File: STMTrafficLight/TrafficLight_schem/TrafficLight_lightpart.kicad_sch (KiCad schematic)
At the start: 66 parts, among them U1 74HC595D, U2 74HC595D, U3 74HC595D

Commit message: Marked connectors and added power LEDs, fixed resistors
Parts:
- removed LED?: Red, LED_SMD:LED_0805_2012Metric, symbol Device:LED
- removed R?: 2k, Resistor_SMD:R_0603_1608Metric, symbol Device:R
- added LED?: Green, LED_SMD:LED_0805_2012Metric, symbol Device:LED
- added R?: 1k, Resistor_SMD:R_0805_2012Metric, symbol Device:R
- R?: value 2k -> 1k; footprint Resistor_SMD:R_0603_1608Metric -> Resistor_SMD:R_0805_2012Metric; Distributor link 1 https://www.mouser.se/ProductDetail/Royalohm/0603WAF2001T5E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 -> https://jlcpcb.com/partdetail/18201-0805W8F1001T5E/C17513; Distributor link 2 (none) -> https://www.mouser.se/ProductDetail/Royalohm/0805W8J0100T5E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; LCSC C22975 -> C17513; Manufacturer part number 0603WAF2001T5E -> 0805W8F1001T5E
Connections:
- net GND: now also LED?.1 (K)
- net at LED?.2 (A): now also R?.2
- net at R?.2: now also LED?.2 (A)
- net PL1_Blue renamed PL1_Yellow
- net PL2_Blue renamed PL2_Yellow
- net USR_LED1 renamed Pwr_LED
- new net Status_debug_LED: R?.1

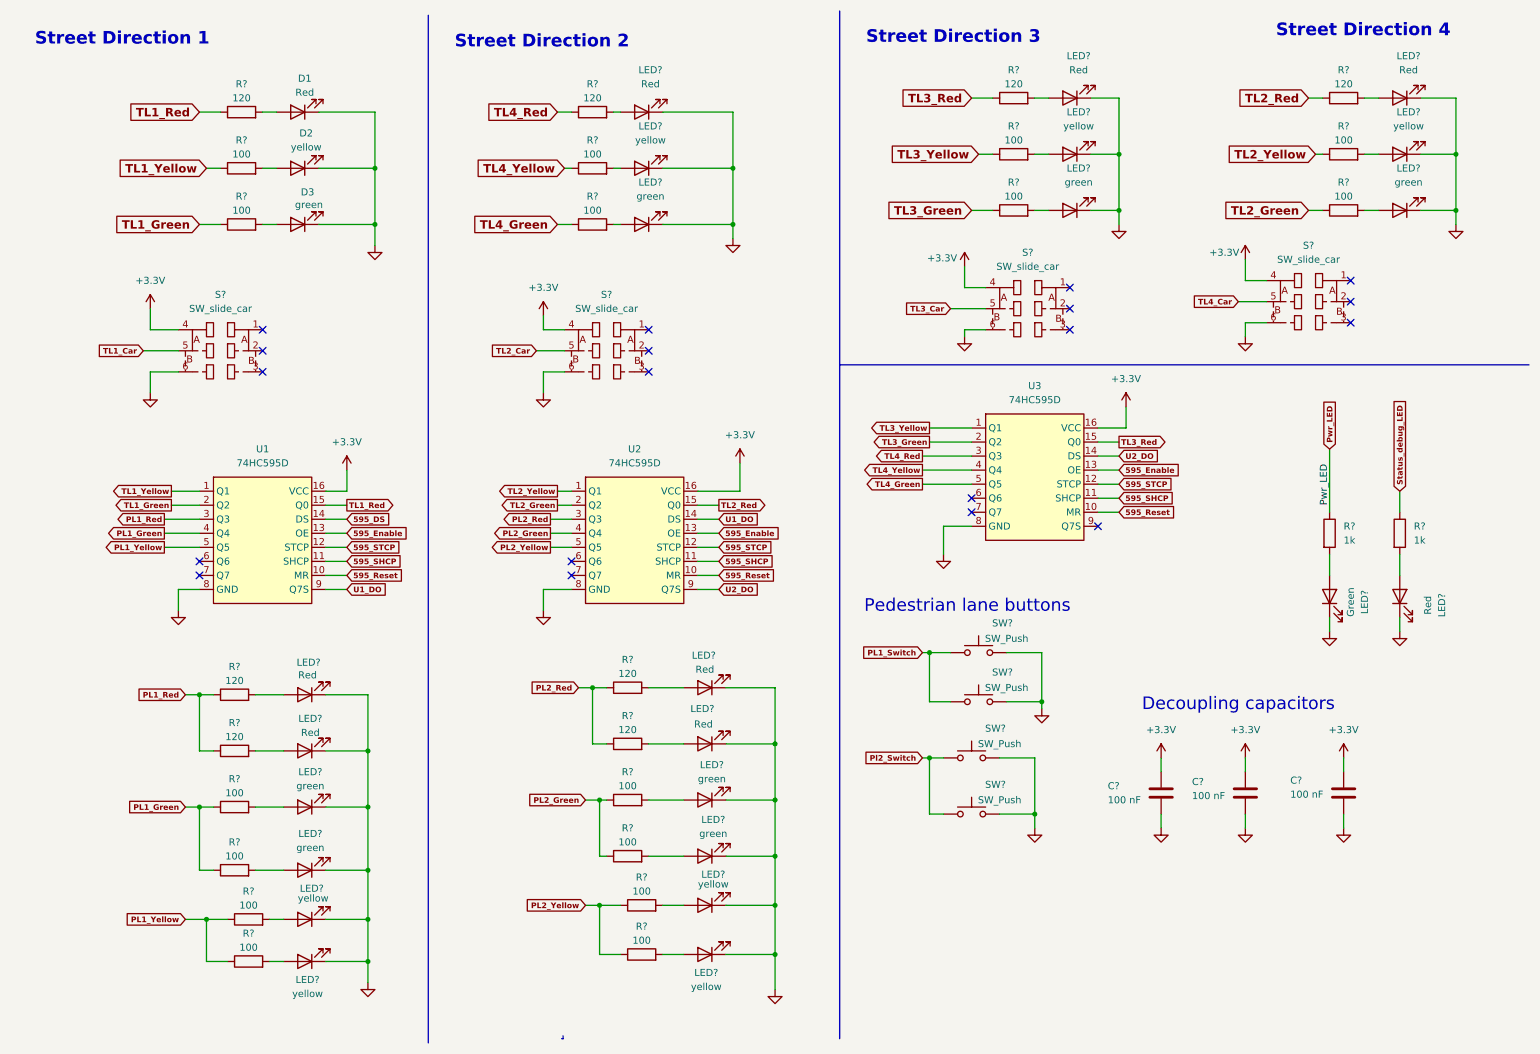
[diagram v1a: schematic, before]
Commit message: Marked connectors and added power LEDs, fixed resistors
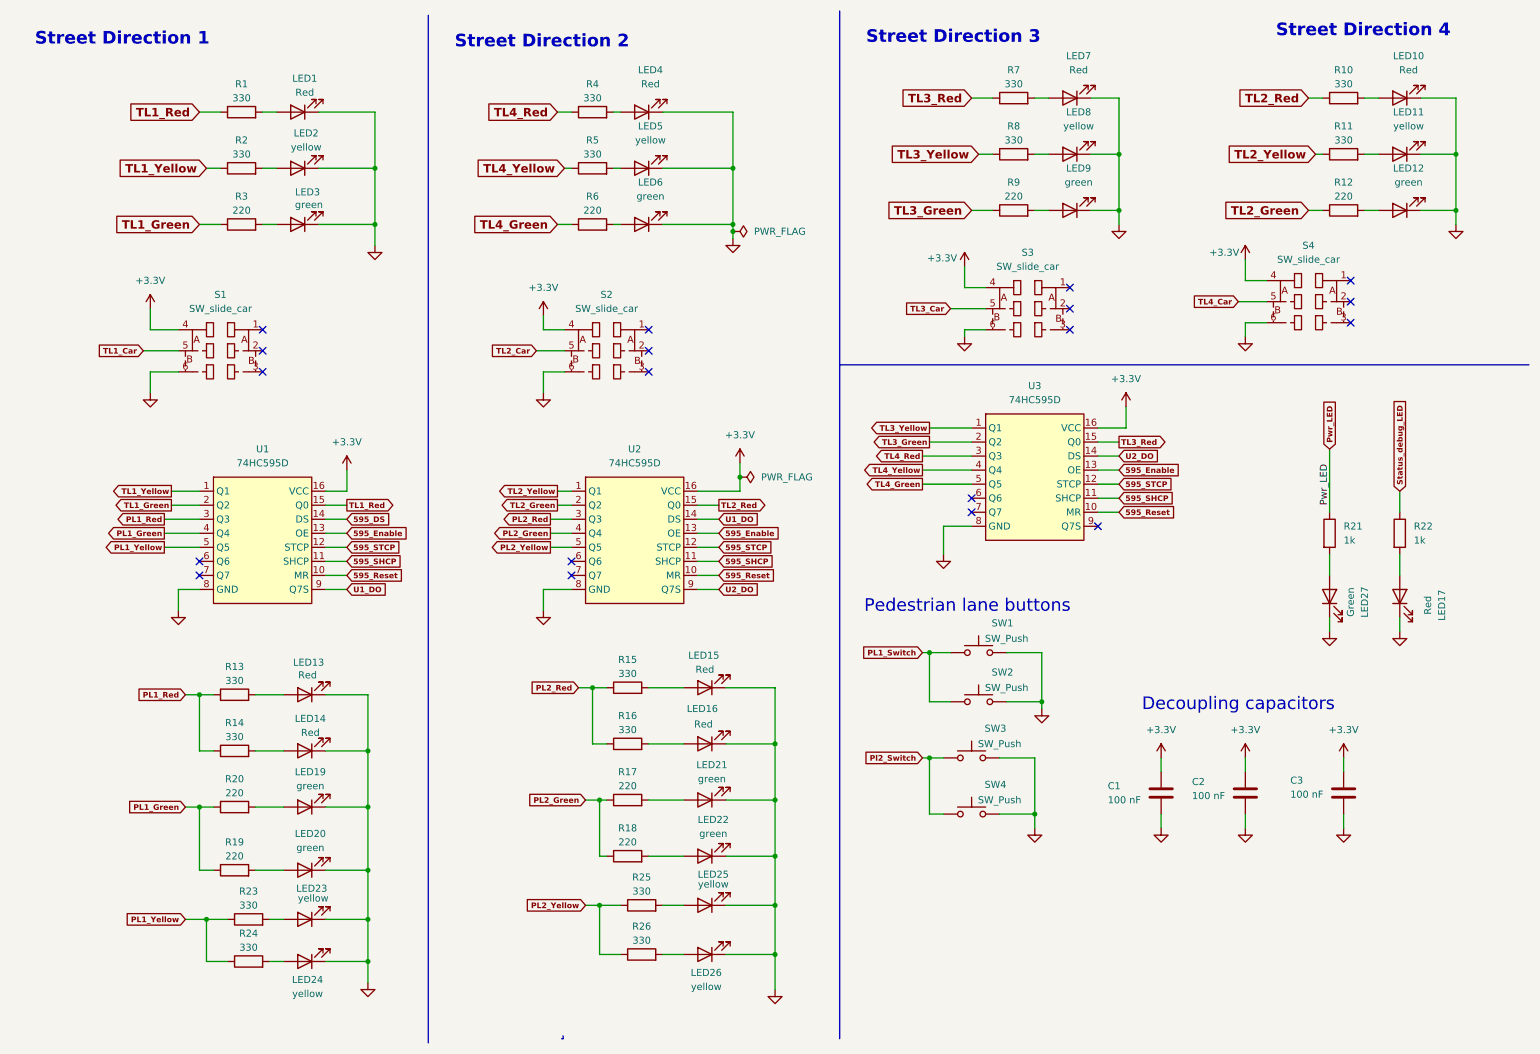
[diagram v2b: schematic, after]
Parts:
- removed R? (x8): 100, Resistor_SMD:R_0603_1608Metric, symbol Device:R
- added R12, R17, R18, R19, R20, R3, R6, R9: 220, Resistor_SMD:R_0805_2012Metric, symbol Device:R
- LED1: renamed from D1; Distributor Link 2 (none) -> https://jlcpcb.com/partdetail/YongyuPhotoelectric-SZYY0805R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
- LED10, LED13, LED14, LED15, LED16, LED17, LED4, LED7: renamed from LED?; Distributor Link 2 (none) -> https://jlcpcb.com/partdetail/YongyuPhotoelectric-SZYY0805R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
- LED11, LED23, LED24, LED25, LED26, LED5, LED8: renamed from LED?; Distributor Link 1 https://www.xonelec.com/mpn/kento/kt0805y -> https://www.xonelec.com/mpn/yongyuphotoelectric/szyy0805y; Distributor Link 2 https://jlcpcb.com/partdetail/YongyuPhotoelectric-SZYY0805Y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 -> https://www.lcsc.com/product-detail/C434436.html; Distributor link 2 (none) -> https://www.lcsc.com/product-detail/C434436.html
- LED2: renamed from D2; Distributor Link 1 https://www.xonelec.com/mpn/kento/kt0805y -> https://www.xonelec.com/mpn/yongyuphotoelectric/szyy0805y; Distributor Link 2 https://jlcpcb.com/partdetail/YongyuPhotoelectric-SZYY0805Y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 -> https://www.lcsc.com/product-detail/C434436.html; Distributor link 2 (none) -> https://www.lcsc.com/product-detail/C434436.html
- R1, R10, R13, R14, R15, R16, R4, R7: renamed from R?; value 120 -> 330; Distributor Link 1 (none) -> https://eu.mouser.com/ProductDetail/Royalohm/0805W8F3300T5E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; Distributor link 1 https://www.mouser.se/ProductDetail/Royalohm/0805W8F1200T5E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 -> https://eu.mouser.com/ProductDetail/Royalohm/0805W8F3300T5E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; Distributor link 2 https://www.lcsc.com/product-detail/C17437.html -> https://www.lcsc.com/product-detail/C17630.html; LCSC C17437 -> C17630; Manufacture Part number 0805W8F1200T5E -> (none); Manufacturer part number (none) -> 0805W8F3300T5E
- R11, R2, R23, R24, R25, R26, R5, R8: renamed from R?; value 100 -> 330; footprint Resistor_SMD:R_0603_1608Metric -> Resistor_SMD:R_0805_2012Metric; Distributor Link 1 (none) -> https://eu.mouser.com/ProductDetail/Royalohm/0805W8F3300T5E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; Distributor link 1 https://www.mouser.se/ProductDetail/Royalohm/0805W8J0100T5E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 -> https://eu.mouser.com/ProductDetail/Royalohm/0805W8F3300T5E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; Distributor link 2 https://www.lcsc.com/product-detail/C17408.html -> https://www.lcsc.com/product-detail/C17630.html; LCSC C17408 -> C17630; Manufacture Part number 0805W8F1000T5E -> (none); Manufacturer part number (none) -> 0805W8F3300T5E
- gave numbers to parts that had none: 21
- renumbered D3 to LED3
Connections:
- net PL1_Green: now also R19.1, R20.1
- net PL2_Green: now also R17.1, R18.1
- net TL1_Green: now also R3.1
- net TL2_Green: now also R12.1
- net TL3_Green: now also R9.1
- net TL4_Green: now also R6.1
- net at LED22.2 (A): now also R18.2
- net at LED9.2 (A): now also R9.2
- net at LED3.2 (A): now also R3.2
- net at LED20.2 (A): now also R19.2
- net at LED21.2 (A): now also R17.2
- net at LED6.2 (A): now also R6.2
- net at LED19.2 (A): now also R20.2
- net at LED12.2 (A): now also R12.2

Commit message: Finally started the PCB design
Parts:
- renumbered C1 to C3, C2 to C4, C3 to C5, LED1 to D1, LED2 to D2, LED3 to D3, LED13 to LED1, LED15 to LED10, LED16 to LED11, LED21 to LED12, LED22 to LED13, LED25 to LED14, LED26 to LED15, LED7 to LED16, LED8 to LED17, LED9 to LED18, LED27 to LED19, LED14 to LED2, LED10 to LED20, LED11 to LED21, LED12 to LED22, LED17 to LED23, LED19 to LED3, LED20 to LED4, LED23 to LED5, LED24 to LED6, LED4 to LED7, LED5 to LED8, LED6 to LED9, R13 to R1, R4 to R10, R5 to R11, R15 to R13, R16 to R14, R25 to R15, R26 to R16, R14 to R2, R7 to R21, R8 to R22, R21 to R23, R10 to R24, R11 to R25, R22 to R26, R1 to R4, R2 to R5, R23 to R7, R24 to R8, SW3 to SW1, SW4 to SW2, SW1 to SW3, SW2 to SW4
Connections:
- net 595_DS renamed 595_DS_SPI1_MOSI
- net 595_SHCP renamed 595_SHCP_SPI1_CLK
- net 595_STCP renamed 595_STCP_RCLK
- net Pl2_Switch renamed PL2_Switch

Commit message: Added silk screen and edge cutouts
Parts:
- added S1: SW_slide_car, Trafficlight_Library:Sw_slide_car, symbol 74HC595_shiftreg_symbol:Sw_slide_car
- renumbered C3 to C1, C4 to C2, C5 to C3, D1 to LED1, LED20 to LED10, LED21 to LED11, LED22 to LED12, LED1 to LED13, LED2 to LED14, LED10 to LED15, LED11 to LED16, LED23 to LED17, LED3 to LED19, D2 to LED2, LED4 to LED20, LED12 to LED21, LED13 to LED22, LED5 to LED23, LED6 to LED24, LED14 to LED25, LED15 to LED26, LED19 to LED27, D3 to LED3, LED7 to LED4, LED8 to LED5, LED9 to LED6, LED16 to LED7, LED17 to LED8, LED18 to LED9, R4 to R1, R24 to R10, R25 to R11, R1 to R13, R2 to R14, R13 to R15, R14 to R16, R5 to R2, R23 to R21, R26 to R22, R7 to R23, R8 to R24, R15 to R25, R16 to R26, R10 to R4, R11 to R5, R21 to R7, R22 to R8, SW3 to SW1, SW4 to SW2, SW1 to SW3, SW2 to SW4
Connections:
- net +3.3V: now also S1.4; no longer S1.4
- net GND: now also S1.6; no longer S1.6
- net TL1_Car: now also S1.5; no longer S1.5
